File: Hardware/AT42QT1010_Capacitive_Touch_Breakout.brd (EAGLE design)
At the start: 25.4 x 33 mm, 31 parts, among them Q1 NPN, U1 AT42QT1010UDFN

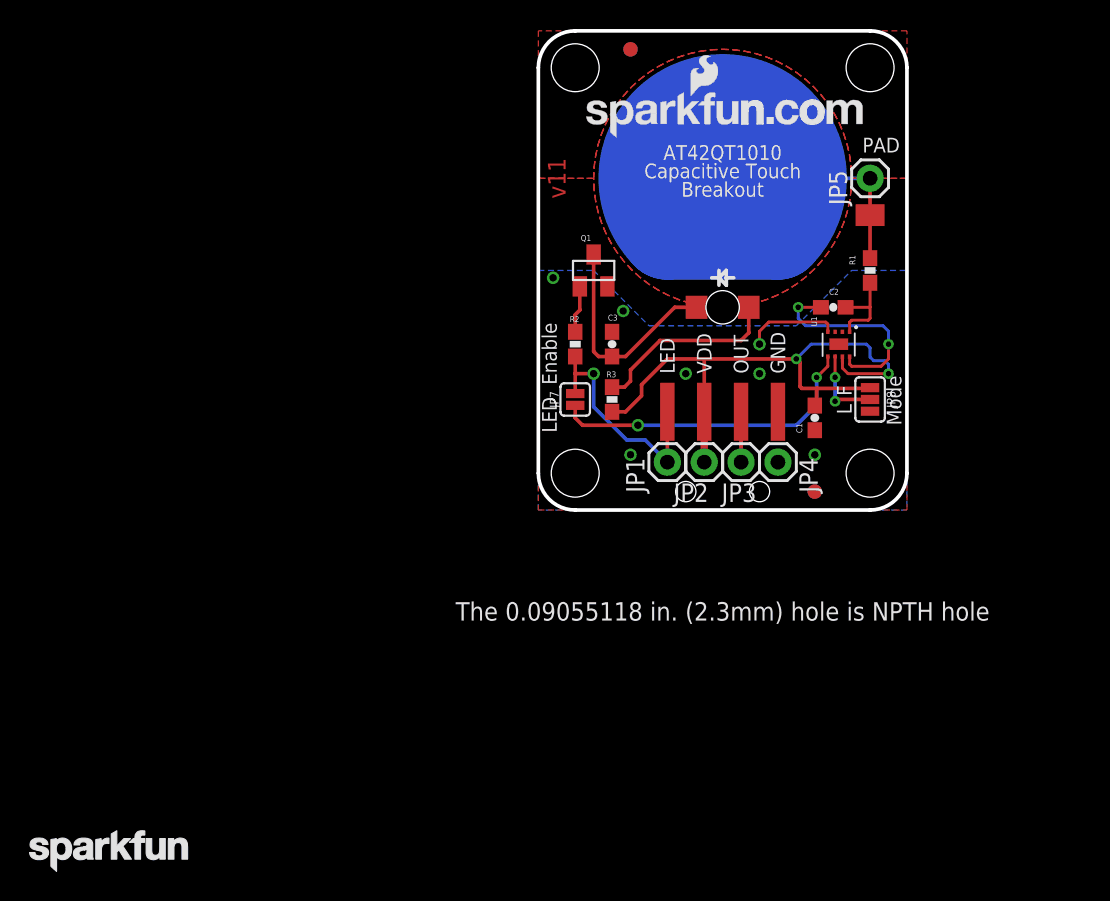
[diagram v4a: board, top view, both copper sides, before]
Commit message: Silk, 0603 packages, flipped header
Fixed some redundant silk, replaced all 0603 packages with newer
versions, and flipped the 4 pin header to align with the PTH headers on
the schematic.
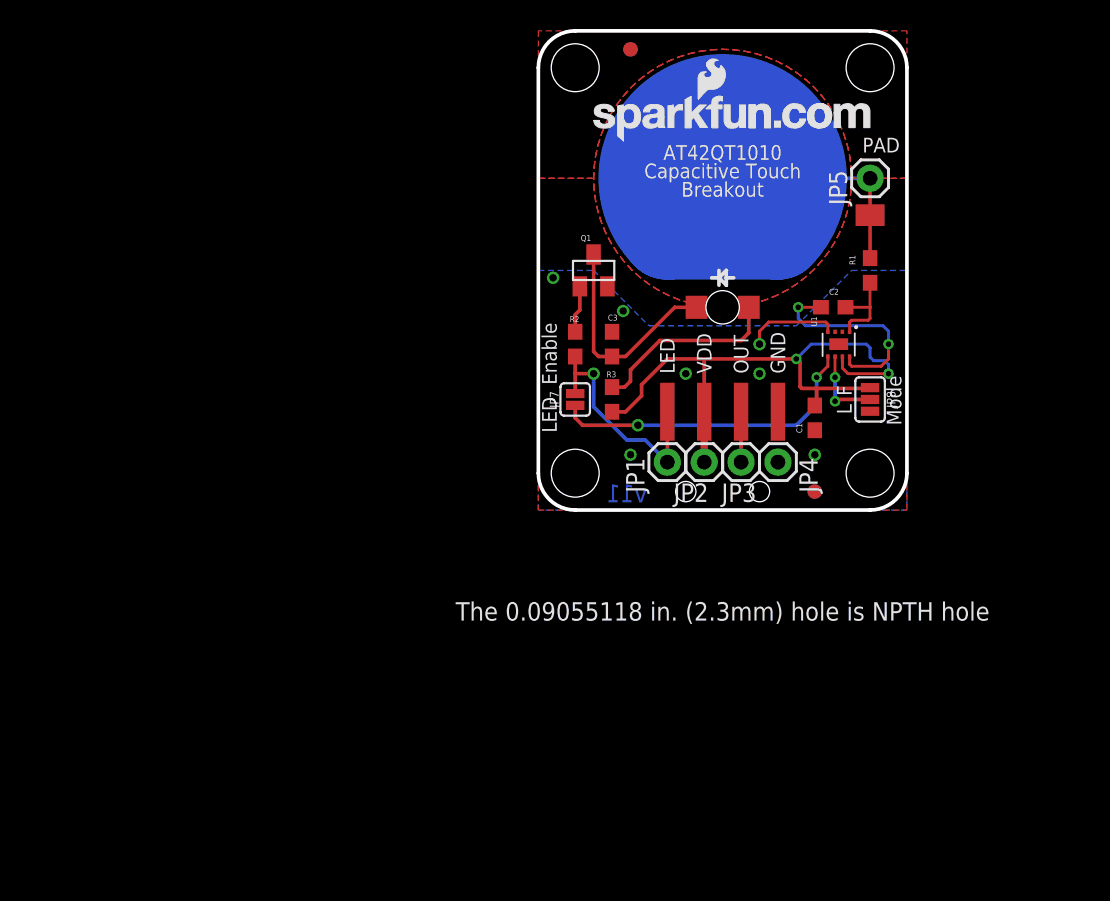
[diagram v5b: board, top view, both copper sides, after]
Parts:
- removed LOGO1: LOGO-SFENEW, SparkFun-Aesthetics:SFE-NEW-WEBLOGO
- removed LOGO4: SFE_LOGO_NAME.1_INCH, SparkFun-Aesthetics:SFE_LOGO_NAME_.1
- added LOGO5: SFE_LOGO_NAME_WEB, SparkFun-Aesthetics:SFE_LOGO_NAME_WEB
- C1, C2, C3: device SparkFun-Capacitors:0603-CAP -> SparkFun-Capacitors:0603
- R1, R2, R3: device SparkFun-Resistors:0603-RES -> SparkFun-Resistors:0603
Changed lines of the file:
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@@
 <layers>
 <layer number="1" name="Top" color="4" fill="1" visible="yes" active="yes"/>
-<layer number="15" name="Route15" color="4" fill="6" visible="yes" active="yes"/>
+<layer number="15" name="Route15" color="4" fill="6" visible="no" active="yes"/>
 <layer number="16" name="Bottom" color="1" fill="1" visible="yes" active="yes"/>
 <layer number="17" name="Pads" color="2" fill="1" visible="yes" active="yes"/>
@@
 <layer number="39" name="tKeepout" color="4" fill="11" visible="no" active="yes"/>
 <layer number="40" name="bKeepout" color="1" fill="11" visible="no" active="yes"/>
-<layer number="41" name="tRestrict" color="4" fill="10" visible="yes" active="yes"/>
-<layer number="42" name="bRestrict" color="1" fill="10" visible="yes" active="yes"/>
-<layer number="43" name="vRestrict" color="2" fill="10" visible="yes" active="yes"/>
+<layer number="41" name="tRestrict" color="4" fill="10" visible="no" active="yes"/>
+<layer number="42" name="bRestrict" color="1" fill="10" visible="no" active="yes"/>
+<layer number="43" name="vRestrict" color="2" fill="10" visible="no" active="yes"/>
 <layer number="44" name="Drills" color="7" fill="1" visible="no" active="yes"/>
 <layer number="45" name="Holes" color="7" fill="1" visible="yes" active="yes"/>
@@
 <layer number="51" name="tDocu" color="6" fill="1" visible="yes" active="yes"/>
 <layer number="52" name="bDocu" color="7" fill="1" visible="no" active="yes"/>
-<layer number="2" name="Route2" color="1" fill="3" visible="yes" active="yes"/>
+<layer number="2" name="Route2" color="1" fill="3" visible="no" active="yes"/>
 <layer number="3" name="Route3" color="4" fill="3" visible="no" active="no"/>
 <layer number="4" name="Route4" color="1" fill="4" visible="no" active="no"/>
@@
 <text x="13.97" y="5.08" size="1.016" layer="22" font="vector" ratio="19" rot="MR270" align="center-right">OUT</text>
 <text x="16.51" y="5.08" size="1.016" layer="22" font="vector" ratio="19" rot="MR270" align="center-right">GND</text>
-<text x="1.27" y="22.86" size="1.2192" layer="1" font="vector" ratio="15" rot="R270" align="center">v11</text>
+<text x="6.096" y="1.143" size="1.2192" layer="16" font="vector" ratio="15" rot="MR0" align="center">v11</text>
 <text x="22.86" y="24.638" size="1.016" layer="22" font="vector" ratio="19" rot="MR270" align="center-right">PAD</text>
 <text x="12.7" y="24.13" size="1.016" layer="21" font="vector" ratio="19" align="bottom-center">AT42QT1010</text>
@@
 <element name="FRAME1" library="SparkFun-Aesthetics" package="CREATIVE_COMMONS" value="FRAME-LETTER" x="-15.24" y="-17.78"/>
 <element name="LOGO2" library="SparkFun-Aesthetics" package="OSHW-LOGO-S" value="OSHW-LOGOS" x="22.86" y="19.05" rot="MR0"/>
-<element name="C1" library="SparkFun-Capacitors" package="0603-CAP" value="0.1uF" x="19.05" y="6.35" smashed="yes" rot="R270">
+<element name="C1" library="SparkFun-Capacitors" package="0603" value="0.1uF" x="19.05" y="6.35" smashed="yes" rot="R270">
 <attribute name="NAME" x="17.78" y="5.969" size="0.4064" layer="25" font="vector" rot="R270"/>
-<attribute name="VALUE" x="17.907" y="7.366" size="0.4064" layer="27" font="vector" rot="R270"/>
-</element>
-<element name="C2" library="SparkFun-Capacitors" package="0603-CAP" value="10nF" x="20.32" y="13.97" smashed="yes" rot="R180">
+<attribute name="VALUE" value="0.1uF" x="17.907" y="7.366" size="0.4064" layer="27" font="vector" rot="R270"/>
+<attribute name="PROD_ID" value="CAP-00810" x="19.05" y="6.35" size="1.778" layer="27" rot="R270" display="off"/>
+</element>
+<element name="C2" library="SparkFun-Capacitors" package="0603" value="10nF" x="20.32" y="13.97" smashed="yes" rot="R180">
 <attribute name="NAME" x="20.701" y="15.24" size="0.4064" layer="25" font="vector" rot="R180"/>
-<attribute name="VALUE" x="21.336" y="15.113" size="0.4064" layer="27" font="vector" rot="R180"/>
-</element>
-<element name="C3" library="SparkFun-Capacitors" package="0603-CAP" value="10nF" x="5.08" y="11.43" smashed="yes" rot="R90">
+<attribute name="VALUE" value="10nF" x="21.336" y="15.113" size="0.4064" layer="27" font="vector" rot="R180"/>
+<attribute name="PROD_ID" value="CAP-00867" x="20.32" y="13.97" size="1.778" layer="27" rot="R180" display="off"/>
+</element>
+<element name="C3" library="SparkFun-Capacitors" package="0603" value="10nF" x="5.08" y="11.43" smashed="yes" rot="R90">
 <attribute name="NAME" x="5.461" y="13.462" size="0.4064" layer="25" font="vector" rot="R180"/>
-<attribute name="VALUE" x="6.223" y="10.414" size="0.4064" layer="27" font="vector" rot="R90"/>
-</element>
-<element name="R1" library="SparkFun-Resistors" package="0603-RES" value="10k" x="22.86" y="16.51" smashed="yes" rot="R90">
+<attribute name="VALUE" value="10nF" x="6.223" y="10.414" size="0.4064" layer="27" font="vector" rot="R90"/>
+<attribute name="PROD_ID" value="CAP-00867" x="5.08" y="11.43" size="1.778" layer="27" rot="R90" display="off"/>
+</element>
+<element name="R1" library="SparkFun-Resistors" package="0603" value="10k" x="22.86" y="16.51" smashed="yes" rot="R90">
 <attribute name="NAME" x="21.844" y="16.891" size="0.4064" layer="25" font="vector" rot="R90"/>
-<attribute name="VALUE" x="24.003" y="15.494" size="0.4064" layer="27" font="vector" rot="R90"/>
-</element>
-<element name="R2" library="SparkFun-Resistors" package="0603-RES" value="2.2k" x="2.54" y="11.43" smashed="yes" rot="R90">
+<attribute name="VALUE" value="10k" x="24.003" y="15.494" size="0.4064" layer="27" font="vector" rot="R90"/>
+<attribute name="PROD_ID" value="RES-00824" x="22.86" y="16.51" size="1.778" layer="27" rot="R90" display="off"/>
+</element>
+<element name="R2" library="SparkFun-Resistors" package="0603" value="2.2k" x="2.54" y="11.43" smashed="yes" rot="R90">
 <attribute name="NAME" x="2.159" y="12.954" size="0.4064" layer="25" font="vector"/>
-<attribute name="VALUE" x="3.683" y="10.414" size="0.4064" layer="27" font="vector" rot="R90"/>
-</element>
-<element name="R3" library="SparkFun-Resistors" package="0603-RES" value="200" x="5.08" y="7.62" smashed="yes" rot="R270">
+<attribute name="VALUE" value="2.2k" x="3.683" y="10.414" size="0.4064" layer="27" font="vector" rot="R90"/>
+<attribute name="PROD_ID" value="RES-08272" x="2.54" y="11.43" size="1.778" layer="27" rot="R90" display="off"/>
+</element>
+<element name="R3" library="SparkFun-Resistors" package="0603" value="200" x="5.08" y="7.62" smashed="yes" rot="R270">
 <attribute name="NAME" x="4.699" y="9.144" size="0.4064" layer="25" font="vector"/>
-<attribute name="VALUE" x="3.937" y="8.636" size="0.4064" layer="27" font="vector" rot="R270"/>
+<attribute name="VALUE" value="200" x="3.937" y="8.636" size="0.4064" layer="27" font="vector" rot="R270"/>
+<attribute name="PROD_ID" value="RES-08220" x="5.08" y="7.62" size="1.778" layer="27" rot="R270" display="off"/>
 </element>
 <element name="Q1" library="SparkFun-DiscreteSemi" package="SOT23" value="NPN" x="3.81" y="16.51">
@@
 <element name="STANDOFF3" library="SparkFun-Electromechanical" package="STAND-OFF" value="STAND-OFF" x="22.86" y="30.48"/>
 <element name="STANDOFF4" library="SparkFun-Electromechanical" package="STAND-OFF" value="STAND-OFF" x="2.54" y="30.48"/>
-<element name="LOGO1" library="SparkFun-Aesthetics" package="SFE-NEW-WEBLOGO" value="LOGO-SFENEW" x="3.302" y="25.654" smashed="yes"/>
 <element name="LOGO3" library="SparkFun-Aesthetics" package="SFE-LOGO-FLAME" value="LOGO-SFESK" x="2.54" y="17.78" rot="MR0"/>
 <element name="JP1" library="SparkFun-Connectors" package="1X01" value="M01PTH" x="8.89" y="3.302" smashed="yes">
@@
 <element name="FID3" library="SparkFun-Aesthetics" package="FIDUCIAL-1X2" value="FIDUCIAL1X2" x="19.05" y="1.27" rot="MR0"/>
 <element name="FID4" library="SparkFun-Aesthetics" package="FIDUCIAL-1X2" value="FIDUCIAL1X2" x="6.35" y="31.75" rot="MR0"/>
-<element name="LOGO4" library="SparkFun-Aesthetics" package="SFE_LOGO_NAME_.1" value="SFE_LOGO_NAME.1_INCH" x="-35.56" y="-25.4"/>
 <element name="JP7" library="SparkFun-Jumpers" package="SMT-JUMPER_2_NO_SILK" value="JUMPER-SMT_2_NO_SILK" x="2.54" y="7.62" rot="R90"/>
+<element name="LOGO5" library="SparkFun-Aesthetics" package="SFE_LOGO_NAME_WEB" value="SFE_LOGO_NAME_WEB" x="3.81" y="25.4"/>
 </elements>
 <signals>
